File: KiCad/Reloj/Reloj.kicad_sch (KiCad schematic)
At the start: 4 parts

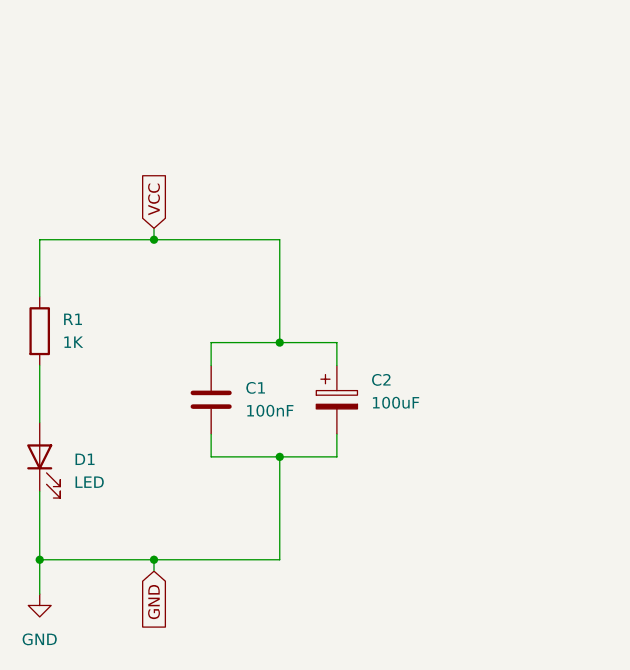
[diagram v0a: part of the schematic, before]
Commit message: Selecciono footprints y disposicion prelimar de PCB
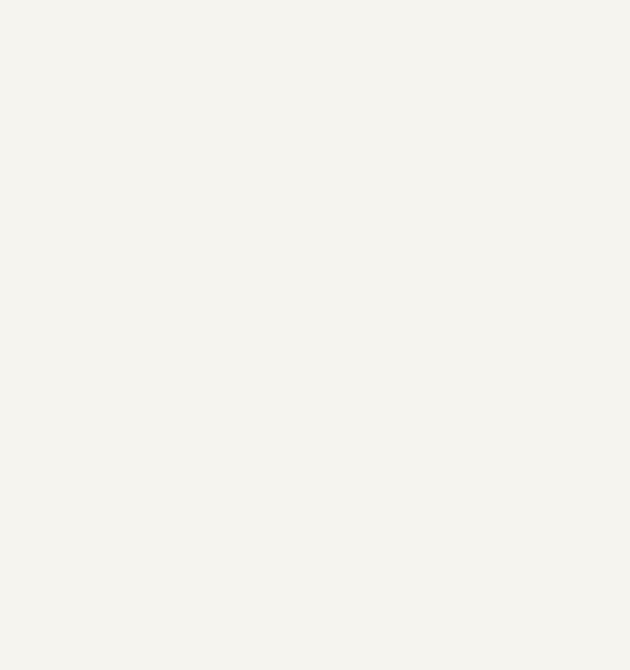
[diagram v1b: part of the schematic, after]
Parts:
- removed C1: 100nF, Capacitor_SMD:C_0805_2012Metric, symbol Device:C
- removed C2: 100uF, Capacitor_SMD:CP_Elec_5x3.9, symbol Device:C_Polarized
- removed D1: LED, LED_SMD:LED_0805_2012Metric_Pad1.15x1.40mm_HandSolder, symbol Device:LED
- removed R1: 1K, Resistor_SMD:R_0805_2012Metric, symbol Device:R
